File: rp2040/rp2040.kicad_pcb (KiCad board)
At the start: 2 copper layers, 47 parts, among them J1 USB_B_Micro, J2 Conn_01x18, J3 Conn_01x02, J4 Conn_01x18, Q1 2N7002, Q2 2N7002, SW1 6x6_SMD_BUTTON, U1 AT24C02C, U2 RP2040, U3 W25Q128JVS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

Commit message: .
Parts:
- removed H1, H2, H3, H4: MountingHole, MountingHole:MountingHole_2.7mm_M2.5
- moved J4 103.1 mm to (164.1, 72.1)
- moved U5 90.5 mm to (143.0, 113.9)
- moved R3 76.8 mm to (133.3, 114.8), turned to 90 degrees
- moved R4 74.9 mm to (135.3, 114.8), turned to 90 degrees
- moved C14 74.1 mm to (144.4, 102.7), turned to -90 degrees
- moved C13 69.6 mm to (140.3, 102.7), turned to 90 degrees
- moved J2 66.8 mm to (120.9, 72.1)
- moved U1 63.4 mm to (141.5, 113.8), turned to 180 degrees
- moved R11 63.1 mm to (142.4, 102.7), turned to -90 degrees
- moved C1 61.1 mm to (139.5, 117.7), turned to 180 degrees
- moved R6 53.5 mm to (110.6, 105.5)
- moved Y1 51.9 mm to (142.4, 106.4), turned to 180 degrees
- moved R5 48.1 mm to (110.6, 97.2), turned to 180 degrees
- moved D1 42.5 mm to (110.5, 103.4), turned to 180 degrees
- moved R8 32.3 mm to (98.2, 86.9), turned to -90 degrees
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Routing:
- net QSPI_SD3: track 0.00 -> 18.7 mm
- net QSPI_SCLK: track 0.00 -> 16.6 mm
- net QSPI_SD0: track 0.00 -> 11.9 mm
- net Net-(U2-USB_DM): track 0.00 -> 6.13 mm
- net Net-(U2-USB_DP): track 0.00 -> 5.61 mm
- net QSPI_SS: track 0.00 -> 4.96 mm
- net QSPI_SD1: track 0.00 -> 4.60 mm
- net QSPI_SD2: track 0.00 -> 4.24 mm

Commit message: edit pcb
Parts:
- added H1: MountingHole, MountingHole:MountingHole_3.2mm_M3_Pad_Via, F.Cu at (122.3, 68.7)
- added H2: MountingHole, MountingHole:MountingHole_3.2mm_M3_Pad_Via, F.Cu at (162.7, 68.7)
- added H3: MountingHole, MountingHole:MountingHole_3.2mm_M3_Pad_Via, F.Cu at (162.7, 128.7)
- added H4: MountingHole, MountingHole:MountingHole_3.2mm_M3_Pad_Via, F.Cu at (122.3, 128.7)
- moved J3 93.1 mm to (149.9, 124.0), turned to 180 degrees
- moved C7 84.4 mm to (153.5, 85.5), turned to 90 degrees
- moved C6 82.8 mm to (151.9, 85.5), turned to 90 degrees
- moved C5 81.3 mm to (150.3, 85.5), turned to 90 degrees
- moved C4 79.9 mm to (148.6, 85.5), turned to 90 degrees
- moved C2 79.4 mm to (143.6, 99.2)
- moved C11 78.7 mm to (150.5, 93.6)
- moved C3 78.6 mm to (147.0, 85.5), turned to 90 degrees
- moved C12 68.4 mm to (139.3, 99.2), turned to 180 degrees
- moved C10 64.6 mm to (134.9, 95.8)
- moved C9 64.4 mm to (134.7, 93.1)
- moved C8 63.7 mm to (134.7, 87.9)
- moved Q1 52.3 mm to (159.3, 119.4)
- moved D1 52.3 mm to (159.2, 122.5)
- moved R6 52.3 mm to (159.3, 124.7)
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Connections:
- net Net-(J1-VBUS) renamed VBUS
- C10 pad 2: Net-(C10-Pad2) -> GND
- C11 pad 2: Net-(C10-Pad2) -> GND
- C5 pad 2: Net-(C10-Pad2) -> GND
- C6 pad 2: Net-(C10-Pad2) -> GND
- C7 pad 2: Net-(C10-Pad2) -> GND
- C8 pad 2: Net-(C10-Pad2) -> GND
- C9 pad 2: Net-(C10-Pad2) -> GND
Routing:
- net GPIO0: track 0.00 -> 92.0 mm
- net GPIO14: track 0.00 -> 89.5 mm, vias 0 -> 1
- net GND: track 0.00 -> 83.7 mm, vias 0 -> 21
- net GPIO1: track 0.00 -> 77.5 mm
- net GPIO2: track 0.00 -> 61.2 mm, vias 0 -> 1
- net GPIO3: track 0.00 -> 58.1 mm, vias 0 -> 1
- net GPIO15: track 0.00 -> 37.9 mm
- net SWCLK: track 0.00 -> 32.8 mm
- net SWD: track 0.00 -> 30.4 mm
- net +1V1: track 0.00 -> 29.5 mm, vias 0 -> 2
- net RUN: track 0.00 -> 28.1 mm
- net GPIO13: track 0.00 -> 26.8 mm
- net GPIO16: track 0.00 -> 26.5 mm
- net GPIO12: track 0.00 -> 25.2 mm
- net GPIO17: track 0.00 -> 24.9 mm
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- added copper zone on F.Cu, net +3.3V
- added copper zone on B.Cu, net GND
- added copper zone on F.Cu, net VBUS
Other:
- board outline added: 47.4 x 66.9 mm

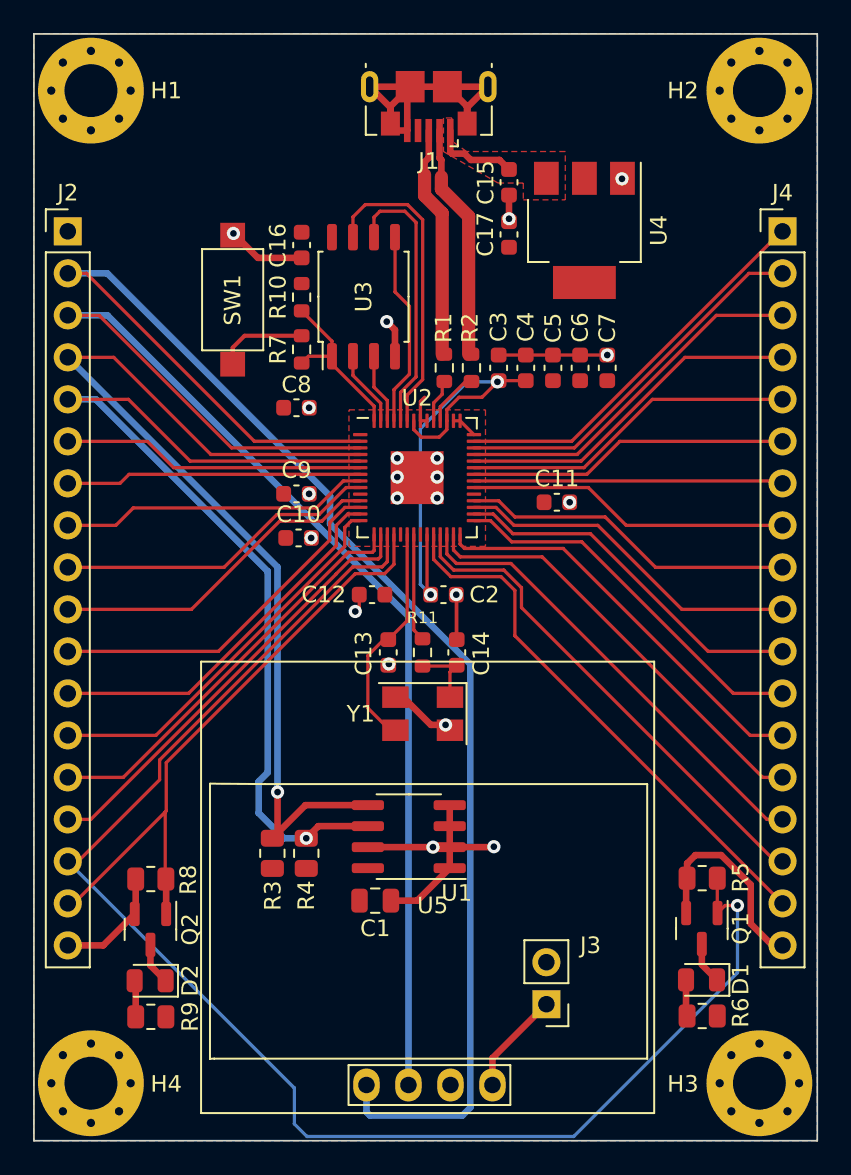
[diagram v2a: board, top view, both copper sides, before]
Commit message: silkscreen fixed
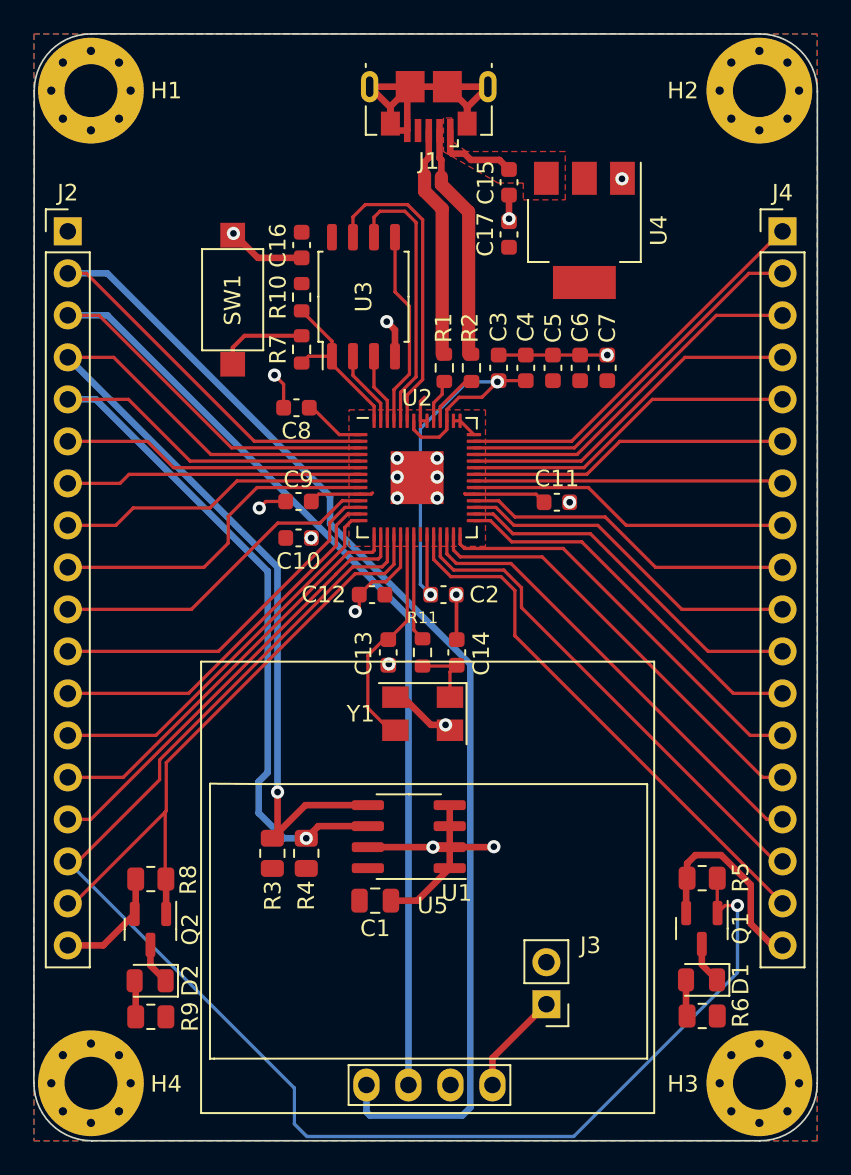
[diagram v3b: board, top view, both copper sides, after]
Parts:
- added G***: LOGO, GOFootprint:ghostman, B.Cu at (142.2, 98.8)
- moved C9 0.48 mm to (134.9, 93.5), turned to 180 degrees
- turned C8 to 180 degrees
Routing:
- net +3.3V: track 3.51 -> 16.2 mm
- net GND: track 83.7 -> 92.8 mm
- net GPIO7: track 19.7 -> 20.6 mm
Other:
- outline, holes or cut-outs redrawn

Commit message: GERBER
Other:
- board text added: "3.3V"
- board text added: "GND"
- board text added: "GPIO0"
- board text added: "GPIO1"
- board text added: "GPIO10"
- board text added: "GPIO11"
- board text added: "GPIO12"
- board text added: "GPIO13"
- board text added: "GPIO14"
- board text added: "GPIO15"
- board text added: "GPIO16"
- board text added: "GPIO17"
- board text added: "GPIO18"
- board text added: "GPIO19"
- board text added: "GPIO2"
- board text added: "GPIO20"
- board text added: "GPIO21"
- board text added: "GPIO22"
- board text added: "GPIO23"
- board text added: "GPIO24"
- board text added: "GPIO25"
- board text added: "GPIO27_ADC0"
- board text added: "GPIO27_ADC1"
- board text added: "GPIO28_ADC2"
- board text added: "GPIO29_ADC3"
- board text added: "GPIO3"
- board text added: "GPIO4"
- board text added: "GPIO5"
- board text added: "GPIO6"
- board text added: "GPIO7"
- board text added: "GPIO8"
- board text added: "GPIO9"
- board text added: "RUN"
- board text added: "SWCLK"
- board text added: "SWD"

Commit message: .
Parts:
- moved C12 5.21 mm to (144.4, 100.4), turned to 0 degrees
- moved C2 0.82 mm to (144.4, 98.9)
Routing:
- net GND: track 92.8 -> 104.8 mm, vias 21 -> 22
- net +3.3V: track 16.2 -> 26.0 mm
- added copper zone on F.Cu, net GND

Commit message: add Reset buton
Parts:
- added R12: 1K, Resistor_SMD:R_0805_2012Metric, F.Cu at (157.5, 126.9)
- added SW2: 6x6_SMD_BUTTON, Button_Switch_SMD:SW_SPST_CK_RS282G05A3, F.Cu at (154.2, 130.1)
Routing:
- net RUN: track 28.1 -> 50.2 mm
- net GND: track 104.8 -> 111.5 mm
- net GPIO14: track 89.5 -> 85.4 mm
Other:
- board text added: "BOOT"
- board text added: "RESET"
